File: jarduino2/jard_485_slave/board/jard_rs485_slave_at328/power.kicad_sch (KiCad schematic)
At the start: 32 parts

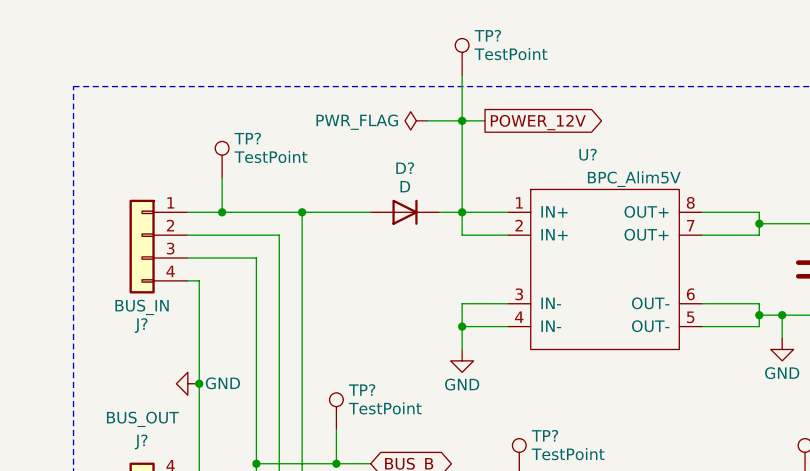
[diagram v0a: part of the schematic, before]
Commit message: Re-routage en gagnant de la place (à finir)
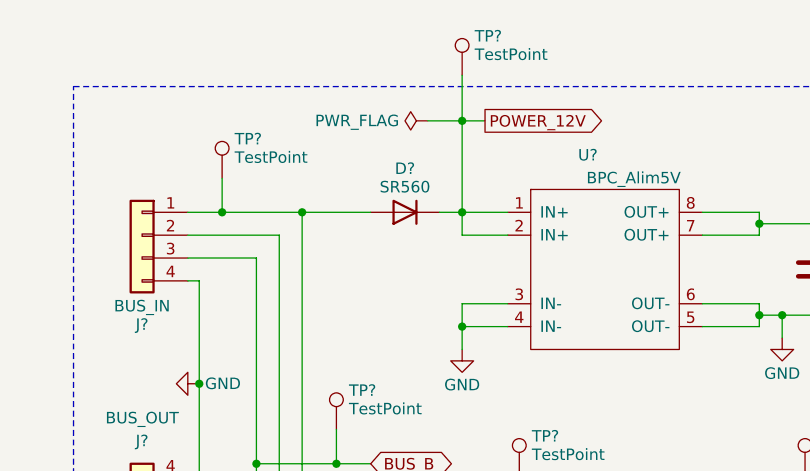
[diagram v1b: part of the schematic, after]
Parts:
- C?: footprint Capacitor_SMD:CP_Elec_5x5.8 -> Capacitor_SMD:CP_Elec_6.3x5.2; Farnell (none) -> 9265759
- D?: value D -> SR560
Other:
- company: (none) -> BPC
- title: (none) -> Carte de commande d'un Oya par RS485
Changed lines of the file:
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@@
 (kicad_sch (version 20230121) (generator eeschema)
   (paper "A4")
+  (title_block
+    (title "Carte de commande d'un Oya par RS485")
+    (date "2024-03-29")
+    (rev "D0")
+    (company "BPC")
+    (comment 1 "Technologie CMD basée sur ATMEGA328")
+    (comment 2 "Monitoring de tension d'alimentation")
+    (comment 3 "1 sortie 12V/5A - 2 entrées TOR - 1 débimètre - 1 LED - Temp -RS485")
+  )
   (junction (at 124.46 39.37) (diameter 0) (color 0 0 0 0)
   )
@@
       (effects (font (size 1.27 1.27)) (justify right))
     )
-    (property "Footprint" "Capacitor_SMD:CP_Elec_5x5.8" (at 129.8448 40.64 0)
+    (property "Footprint" "Capacitor_SMD:CP_Elec_6.3x5.2" (at 129.8448 40.64 0)
       (effects (font (size 1.27 1.27)) hide)
     )
     (property "Datasheet" "~" (at 130.81 44.45 0)
+      (effects (font (size 1.27 1.27)) hide)
+    )
+    (property "Farnell" "9265759" (at 130.81 44.45 0)
       (effects (font (size 1.27 1.27)) hide)
     )
@@
       (effects (font (size 1.27 1.27)))
     )
-    (property "Value" "D" (at 72.39 35.298 0)
-      (effects (font (size 1.27 1.27)))
-    )
+    (property "Value" "SR560" (at 72.39 35.298 0)
+      (effects (font (size 1.27 1.27)))
+    )

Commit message: Petites coquilles de dossier
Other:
- title: Carte de commande d'un Oya par RS485 -> Carte de commande d'un OYA par RS485
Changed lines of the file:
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@@
   (paper "A4")
   (title_block
-    (title "Carte de commande d'un Oya par RS485")
+    (title "Carte de commande d'un OYA par RS485")
     (date "2024-03-29")
     (rev "D0")
     (company "BPC")
-    (comment 1 "Technologie CMD basée sur ATMEGA328")
+    (comment 1 "Technologie CMS basée sur ATMEGA328")
     (comment 2 "Monitoring de tension d'alimentation")
-    (comment 3 "1 sortie 12V/5A - 2 entrées TOR - 1 débimètre - 1 LED - Temp -RS485")
+    (comment 3 "1 sortie 12V/5A - 2 entrées TOR - 1 débimètre - 1 LED - Temp - RS485")
   )
   (junction (at 124.46 39.37) (diameter 0) (color 0 0 0 0)

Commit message: Suite revue: - Retrait limiteur de courant NOK pour flowmeter - Résolution des erreurs PCB
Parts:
- C?: footprint Capacitor_SMD:CP_Elec_6.3x5.2 -> Capacitor_SMD:CP_Elec_5x5.9; Fabricant (none) -> CHEMI-CON: EMZA350ADA100ME61G; Farnell 9265759 -> 1698723
- U?: Farnell (none) -> 2519414
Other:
- title: Carte de commande d'un OYA par RS485 -> Carte de commande d'un OYA - Esclave RS485
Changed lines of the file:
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@@
   (paper "A4")
   (title_block
-    (title "Carte de commande d'un OYA par RS485")
-    (date "2024-03-29")
+    (title "Carte de commande d'un OYA - Esclave RS485")
+    (date "2024-03-31")
     (rev "D0")
     (company "BPC")
@@
     )
     (property "Datasheet" "https://datasheets.maximintegrated.com/en/ds/MAX1487E-MAX491E.pdf" (at 77.47 135.89 0)
+      (effects (font (size 1.27 1.27)) hide)
+    )
+    (property "Farnell" "2519414" (at 77.47 137.16 0)
       (effects (font (size 1.27 1.27)) hide)
     )
@@
       (effects (font (size 1.27 1.27)) (justify right))
     )
-    (property "Footprint" "Capacitor_SMD:CP_Elec_6.3x5.2" (at 129.8448 40.64 0)
+    (property "Footprint" "Capacitor_SMD:CP_Elec_5x5.9" (at 129.8448 40.64 0)
       (effects (font (size 1.27 1.27)) hide)
     )
@@
       (effects (font (size 1.27 1.27)) hide)
     )
-    (property "Farnell" "9265759" (at 130.81 44.45 0)
-      (effects (font (size 1.27 1.27)) hide)
-    )
+    (property "Farnell" "1698723" (at 130.81 44.45 0)
+      (effects (font (size 1.27 1.27)) hide)
+    )
+    (property "Fabricant" "CHEMI-CON: EMZA350ADA100ME61G" (at 130.81 44.45 0)
+      (effects (font (size 1.27 1.27)) hide)
+    )

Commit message: Correction erreur de MOS (N au lieu de P) + Saisie complete de la BOM
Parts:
- C? (x6): Fabricant (none) -> KEMET; Fournisseur (none) -> Farnell; RefFabricant (none) -> C0603X102J5GACAUTO; RefFournisseur (none) -> 2219417
- C?: Fabricant CHEMI-CON: EMZA350ADA100ME61G -> CHEMI-CON; Farnell 1698723 -> (none); Fournisseur (none) -> Farnell; RefFabricant (none) -> EMZA350ADA100ME61G; RefFournisseur (none) -> 1698723
- D11, D12: Fabricant (none) -> DIODES INC; Fournisseur (none) -> Farnell; RefFabricant (none) -> SD12-7; RefFournisseur (none) -> 3945781RL
- D15: Fabricant (none) -> SEMTECH; Fournisseur (none) -> Farnell; RefFabricant (none) -> SM712.TCT; RefFournisseur (none) -> 1456395RL
- D?: Fabricant (none) -> MULTICOMP PRO; Fournisseur (none) -> Farnell; RefFabricant (none) -> BAV99; RefFournisseur (none) -> 2675152
- D?: Fabricant (none) -> MULTICOMP PRO; Fournisseur (none) -> Farnell; RefFabricant (none) -> SR560; RefFournisseur (none) -> 2675411
- J? (x2): Fabricant (none) -> PHOENIX CONTACT; Fournisseur (none) -> Farnell; RefFabricant (none) -> 1725672; RefFournisseur (none) -> 3041414
- R? (x3): Fabricant (none) -> VISHAY; Fournisseur (none) -> Farnell; RefFabricant (none) -> CRCW0805100RFKTA; RefFournisseur (none) -> 2826073
- R?: Fabricant (none) -> VISHAY; Fournisseur (none) -> Farnell; RefFabricant (none) -> CRCW080540K0FKEA; RefFournisseur (none) -> 3975002
- R?: Fabricant (none) -> MULTICOMP PRO; Fournisseur (none) -> Farnell; RefFabricant (none) -> MCHVR05JTEW1003; RefFournisseur (none) -> 2826073
- S1: Fabricant (none) -> CUI Devices; Purchase-URL (none) -> https://www.digikey.at/en/products/detail/cui-devices/RDS-1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; RefFabricant (none) -> RDS-16S-74385-SMT-TR
- U?: Fabricant (none) -> ANALOG DEVICES; Farnell 2519414 -> (none); Fournisseur (none) -> Farnell; RefFabricant (none) -> MAX3085CSA+T; RefFournisseur (none) -> 2798956

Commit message: Ajout des prix des composants
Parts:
- C? (x6): Price (none) -> 0,42
- C?: Price (none) -> 0,6312
- D11, D12: Price (none) -> 0,1272
- D15: Price (none) -> 1,1964
- D?: Price (none) -> 0,0994
- D?: Price (none) -> 0,5844
- J? (x2): Price (none) -> 2,532
- R? (x3): Price (none) -> 0,0522; RefFournisseur 2826073 -> 1652906
- R?: Price (none) -> 0,0505
- R?: Price (none) -> 0,0522
- S1: Fournisseur (none) -> Digikey; Price None -> 2,76
- TP? (x10): Price (none) -> 0
- U?: Price (none) -> 4,86
- U?: Fournisseur (none) -> Ali express; Price (none) -> 1; Purchase-URL (none) -> https://fr.aliexpress.com/item/1005004858762563.html?spm=a2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; RefFournisseur (none) -> MINI560
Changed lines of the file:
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@@
+      (effects (font (size 1.27 1.27)) hide)
+    )
+    (property "Price" "0" (at 116.84 67.31 0)
       (effects (font (size 1.27 1.27)) hide)
     )
@@
       (effects (font (size 1.27 1.27)) hide)
     )
+    (property "Price" "0,42" (at 48.26 166.37 0)
+      (effects (font (size 1.27 1.27)) hide)
+    )
     (pin "1")
     (pin "2")
@@
     )
     (property "Fabricant" "ANALOG DEVICES" (at 77.47 137.16 0)
+      (effects (font (size 1.27 1.27)) hide)
+    )
+    (property "Price" "4,86" (at 77.47 137.16 0)
       (effects (font (size 1.27 1.27)) hide)
     )
@@
       (effects (font (size 1.27 1.27)) hide)
     )
-    (property "RefFournisseur" "2826073" (at 35.56 160.02 0)
+    (property "RefFournisseur" "1652906" (at 35.56 160.02 0)
       (effects (font (size 1.27 1.27)) hide)
     )
@@
     )
     (property "Description" "Résistance 100 Ohms" (at 35.56 160.02 0)
+      (effects (font (size 1.27 1.27)) hide)
+    )
+    (property "Price" "0,0522" (at 35.56 160.02 0)
       (effects (font (size 1.27 1.27)) hide)
     )
@@
       (effects (font (size 1.27 1.27)) hide)
     )
+    (property "Price" "0,42" (at 68.58 113.03 0)
+      (effects (font (size 1.27 1.27)) hide)
+    )
     (pin "1")
     (pin "2")
@@
       (effects (font (size 1.27 1.27)) hide)
     )
+    (property "Price" "0,1272" (at 129.54 138.43 0)
+      (effects (font (size 1.27 1.27)) hide)
+    )
     (pin "1")
     (pin "2")
@@
     )
     (property "Description" "Condensateur céramique 1nF" (at 38.1 119.38 0)
+      (effects (font (size 1.27 1.27)) hide)
+    )
+    (property "Price" "0,42" (at 38.1 119.38 0)
       (effects (font (size 1.27 1.27)) hide)
     )
@@
       (effects (font (size 1.27 1.27)) hide)
     )
+    (property "Price" "2,532" (at 43.18 72.39 0)
+      (effects (font (size 1.27 1.27)) hide)
+    )
     (pin "1")
     (pin "2")
@@
     )
     (property "Description" "Condensateur céramique 1nF" (at 68.58 123.19 0)
+      (effects (font (size 1.27 1.27)) hide)
+    )
+    (property "Price" "0,42" (at 68.58 123.19 0)
       (effects (font (size 1.27 1.27)) hide)
     )
@@
       (effects (font (size 1.27 1.27)) hide)
     )
+    (property "Price" "0,0505" (at 212.09 36.83 0)
+      (effects (font (size 1.27 1.27)) hide)
+    )
     (pin "1")
     (pin "2")
@@
       (effects (font (size 1.27 1.27)) hide)
     )
+    (property "Price" "0,0994" (at 228.6 36.83 0)
+      (effects (font (size 1.27 1.27)) hide)
+    )
     (pin "1")
     (pin "2")
@@
     )
     (property "Description" "Diode TVS" (at 106.68 138.43 0)
+      (effects (font (size 1.27 1.27)) hide)
+    )
+    (property "Price" "1,1964" (at 106.68 138.43 0)
       (effects (font (size 1.27 1.27)) hide)
     )
@@
       (effects (font (size 1.27 1.27)) hide)
     )
+    (property "Price" "0,6312" (at 130.81 44.45 0)
+      (effects (font (size 1.27 1.27)) hide)
+    )
     (pin "1")
     (pin "2")
@@
       (effects (font (size 1.27 1.27)) (justify bottom) hide)
     )
-    (property "Price" "None" (at 228.6 129.54 0)
+    (property "Price" "2,76" (at 228.6 129.54 0)
       (effects (font (size 1.27 1.27)) (justify bottom) hide)
     )
@@
     )
     (property "Purchase-URL" "https://www.digikey.at/en/products/detail/cui-devices/RDS-16S-74385-SMT-TR/13530571" (at 228.6 129.54 0)
+      (effects (font (size 1.27 1.27)) hide)
+    )
+    (property "Fournisseur" "Digikey" (at 228.6 129.54 0)
       (effects (font (size 1.27 1.27)) hide)
     )
@@
       (effects (font (size 1.27 1.27)) hide)
     )
+    (property "Price" "0" (at 229.87 58.42 0)
+      (effects (font (size 1.27 1.27)) hide)
+    )
     (pin "1")
     (instances
@@
       (effects (font (size 1.27 1.27)) hide)
     )
+    (property "Price" "0,42" (at 118.11 44.45 0)
+      (effects (font (size 1.27 1.27)) hide)
+    )
     (pin "1")
     (pin "2")
@@
       (effects (font (size 1.27 1.27)) hide)
     )
+    (property "Price" "0,5844" (at 72.39 38.1 0)
+      (effects (font (size 1.27 1.27)) hide)
+    )
     (pin "1")
     (pin "2")
@@
     )
     (property "RefFournisseur" "" (at 64.77 62.23 0)
+      (effects (font (size 1.27 1.27)) hide)
+    )
+    (property "Price" "0" (at 64.77 62.23 0)
       (effects (font (size 1.27 1.27)) hide)
     )
@@
       (effects (font (size 1.27 1.27)) hide)
     )
-    (property "RefFournisseur" "2826073" (at 36.83 138.43 0)
+    (property "RefFournisseur" "1652906" (at 36.83 138.43 0)
       (effects (font (size 1.27 1.27)) hide)
     )
@@
       (effects (font (size 1.27 1.27)) hide)
     )
+    (property "Price" "0,0522" (at 36.83 138.43 0)
+      (effects (font (size 1.27 1.27)) hide)
+    )
     (pin "1")
     (pin "2")
@@
     )
     (property "RefFournisseur" "" (at 31.75 134.62 0)
+      (effects (font (size 1.27 1.27)) hide)
+    )
+    (property "Price" "0" (at 31.75 134.62 0)
       (effects (font (size 1.27 1.27)) hide)
     )
@@
       (effects (font (size 1.27 1.27)) hide)
     )
+    (property "Price" "0" (at 124.46 33.02 0)
+      (effects (font (size 1.27 1.27)) hide)
+    )
     (pin "1")
     (instances
@@
       (effects (font (size 1.27 1.27)) hide)
     )
+    (property "Price" "0" (at 52.07 34.29 0)
+      (effects (font (size 1.27 1.27)) hide)
+    )
     (pin "1")
     (instances
@@
       (effects (font (size 1.27 1.27)) hide)
     )
+    (property "Price" "0" (at 85.09 67.31 0)
+      (effects (font (size 1.27 1.27)) hide)
+    )
     (pin "1")
     (instances
@@
       (effects (font (size 1.27 1.27)) hide)
     )
-    (property "RefFournisseur" "2826073" (at 44.45 113.03 0)
+    (property "RefFournisseur" "1652906" (at 44.45 113.03 0)
       (effects (font (size 1.27 1.27)) hide)
     )
@@
     )
     (property "Description" "Résistance 100 Ohms" (at 44.45 113.03 0)
+      (effects (font (size 1.27 1.27)) hide)
+    )
+    (property "Price" "0,0522" (at 44.45 113.03 0)
       (effects (font (size 1.27 1.27)) hide)
     )
@@
       (effects (font (size 1.27 1.27)) hide)
     )
+    (property "Price" "2,532" (at 43.18 40.64 0)
+      (effects (font (size 1.27 1.27)) hide)
+    )
     (pin "1")
     (pin "2")
@@
       (effects (font (size 1.27 1.27)) hide)
     )
+    (property "Price" "0" (at 30.48 156.21 0)
+      (effects (font (size 1.27 1.27)) hide)
+    )
     (pin "1")
     (instances
@@
       (effects (font (size 1.27 1.27)) hide)
     )
+    (property "Price" "0,1272" (at 86.36 118.11 0)
+      (effects (font (size 1.27 1.27)) hide)
+    )
     (pin "1")
     (pin "2")
@@
     )
     (property "RefFournisseur" "" (at 78.74 22.86 0)
+      (effects (font (size 1.27 1.27)) hide)
+    )
+    (property "Price" "0" (at 78.74 22.86 0)
       (effects (font (size 1.27 1.27)) hide)
     )
@@
     )
     (property "RefFournisseur" "" (at 30.48 110.49 0)
+      (effects (font (size 1.27 1.27)) hide)
+    )
+    (property "Price" "0" (at 30.48 110.49 0)
       (effects (font (size 1.27 1.27)) hide)
     )
@@
       (effects (font (size 1.27 1.27)) hide)
     )
+    (property "Price" "0,0522" (at 218.44 29.21 0)
+      (effects (font (size 1.27 1.27)) hide)
+    )
     (pin "1")
     (pin "2")
@@
     )
     (property "Description" "Condensateur céramique 1nF" (at 48.26 146.05 0)
+      (effects (font (size 1.27 1.27)) hide)
+    )
+    (property "Price" "0,42" (at 48.26 146.05 0)
       (effects (font (size 1.27 1.27)) hide)
     )
@@
       (effects (font (size 1.27 1.27)) hide)
     )
-    (property "RefFournisseur" "" (at 86.36 38.1 0)
+    (property "RefFournisseur" "MINI560" (at 86.36 38.1 0)
       (effects (font (size 1.27 1.27)) hide)
     )
@@
       (effects (font (size 1.27 1.27)) hide)
     )
+    (property "Fournisseur" "Ali express" (at 86.36 38.1 0)
+      (effects (font (size 1.27 1.27)) hide)
+    )
+    (property "Price" "1" (at 86.36 38.1 0)
+      (effects (font (size 1.27 1.27)) hide)
+    )
+    (property "Purchase-URL" "https://fr.aliexpress.com/item/1005004858762563.html?spm=a2g0o.productlist.main.79.480fJCb1JCb1eK&algo_pvid=451e0482-3943-4afe-9b18-c6fbc5b1e498&aem_p4p_detail=202404060223422123079384549750008147392&algo_exp_id=451e0482-3943-4afe-9b18-c6fbc5b1e498-39&pdp_npi=4%40dis%21EUR%211.00%211.00%21%21%211.06%211.06%21%40210386d117123954225995359ebc5b%2112000030776865700%21sea%21FR%212150986022%21&curPageLogUid=75SrR34WZyaH&utparam-url=scene%3Asearch%7Cquery_from%3A&search_p4p_id=202404060223422123079384549750008147392_11" (at 86.36 38.1 0)
+      (effects (font (size 1.27 1.27)) hide)
+    )

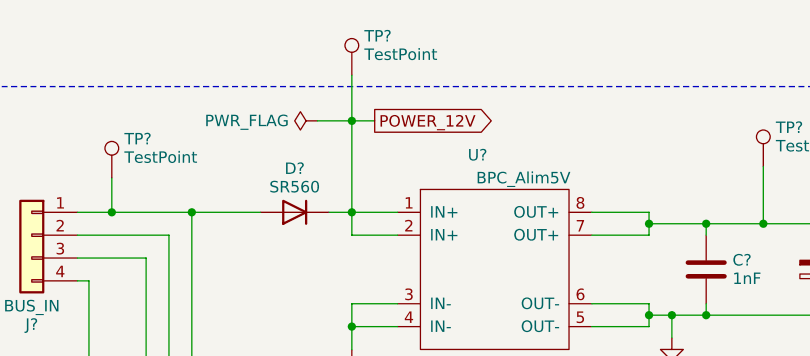
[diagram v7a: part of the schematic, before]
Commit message: Changement empreinte de D2 (trous + gros et 12mm long) Dessin sérigraphie J2 (sens de la sonde)
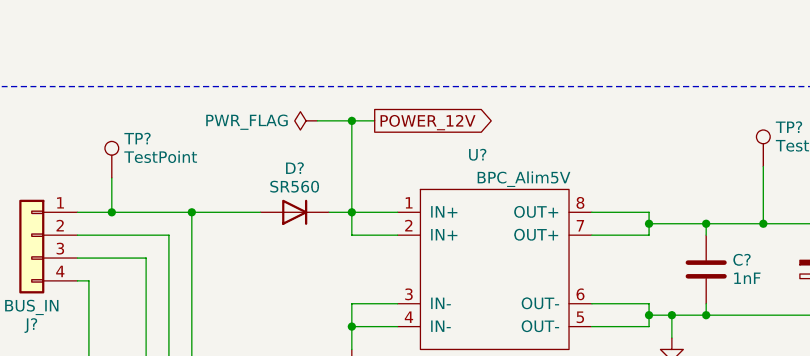
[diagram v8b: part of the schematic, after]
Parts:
- removed TP?: TestPoint, TestPoint:TestPoint_Pad_D1.5mm, symbol Connector:TestPoint
- C?: RefFabricant C0603X102J5GACAUTO -> C0603C104K1RACTU; RefFournisseur 2219417 -> 4199453
- D?: footprint Diode_THT:D_A-405_P7.62mm_Horizontal -> Diode_THT:D_DO-15_P12.70mm_Horizontal
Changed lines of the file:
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@@
-    (stroke (width 0) (type default))
-  )
-  (wire (pts (xy 78.74 22.86) (xy 78.74 27.94))
     (stroke (width 0) (type default))
   )
@@
       (effects (font (size 1.27 1.27)) hide)
     )
-    (property "RefFabricant" "C0603X102J5GACAUTO" (at 68.58 113.03 0)
-      (effects (font (size 1.27 1.27)) hide)
-    )
-    (property "RefFournisseur" "2219417" (at 68.58 113.03 0)
+    (property "RefFabricant" "C0603C104K1RACTU" (at 68.58 113.03 0)
+      (effects (font (size 1.27 1.27)) hide)
+    )
+    (property "RefFournisseur" "4199453" (at 68.58 113.03 0)
       (effects (font (size 1.27 1.27)) hide)
     )
@@
       (effects (font (size 1.27 1.27)))
     )
-    (property "Footprint" "Diode_THT:D_A-405_P7.62mm_Horizontal" (at 72.39 38.1 0)
+    (property "Footprint" "Diode_THT:D_DO-15_P12.70mm_Horizontal" (at 72.39 38.1 0)
       (effects (font (size 1.27 1.27)) hide)
     )
@@
         )
       )
-    )
-  )
-  (symbol (lib_id "Connector:TestPoint") (at 78.74 22.86 0) (unit 1)
-    (in_bom yes) (on_board yes) (dnp no) (fields_autoplaced)
-    (property "Reference" "TP?" (at 80.137 18.534 0)
-      (effects (font (size 1.27 1.27)) (justify left))
-    )
-    (property "Value" "TestPoint" (at 80.137 20.582 0)
-      (effects (font (size 1.27 1.27)) (justify left))
-    )
-    (property "Footprint" "TestPoint:TestPoint_Pad_D1.5mm" (at 83.82 22.86 0)
-      (effects (font (size 1.27 1.27)) hide)
-    )
-    (property "Datasheet" "~" (at 83.82 22.86 0)
-      (effects (font (size 1.27 1.27)) hide)
-    )
-    (property "RefFabricant" "" (at 78.74 22.86 0)
-      (effects (font (size 1.27 1.27)) hide)
-    )
-    (property "RefFournisseur" "" (at 78.74 22.86 0)
-      (effects (font (size 1.27 1.27)) hide)
-    )
-    (property "Price" "0" (at 78.74 22.86 0)
-      (effects (font (size 1.27 1.27)) hide)
-    )
-    (pin "1")
-    (instances
-      (project "jard_rs485_slave_at328"
-        (path "/5ae93d62-0543-4c0e-b37d-d67af6219e1b/36e9fbeb-2032-4e73-95af-53e316cf916d"
-          (reference "TP?") (unit 1)
-        )
-        (path "/5ae93d62-0543-4c0e-b37d-d67af6219e1b/dd36e5af-5314-42bf-9b88-ba8e41ec06f7"
-          (reference "TP5") (unit 1)
-        )
-      )
